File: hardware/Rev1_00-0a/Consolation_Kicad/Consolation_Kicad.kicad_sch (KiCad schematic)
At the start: 35 parts, among them Q14 SSM3K56FS,LF

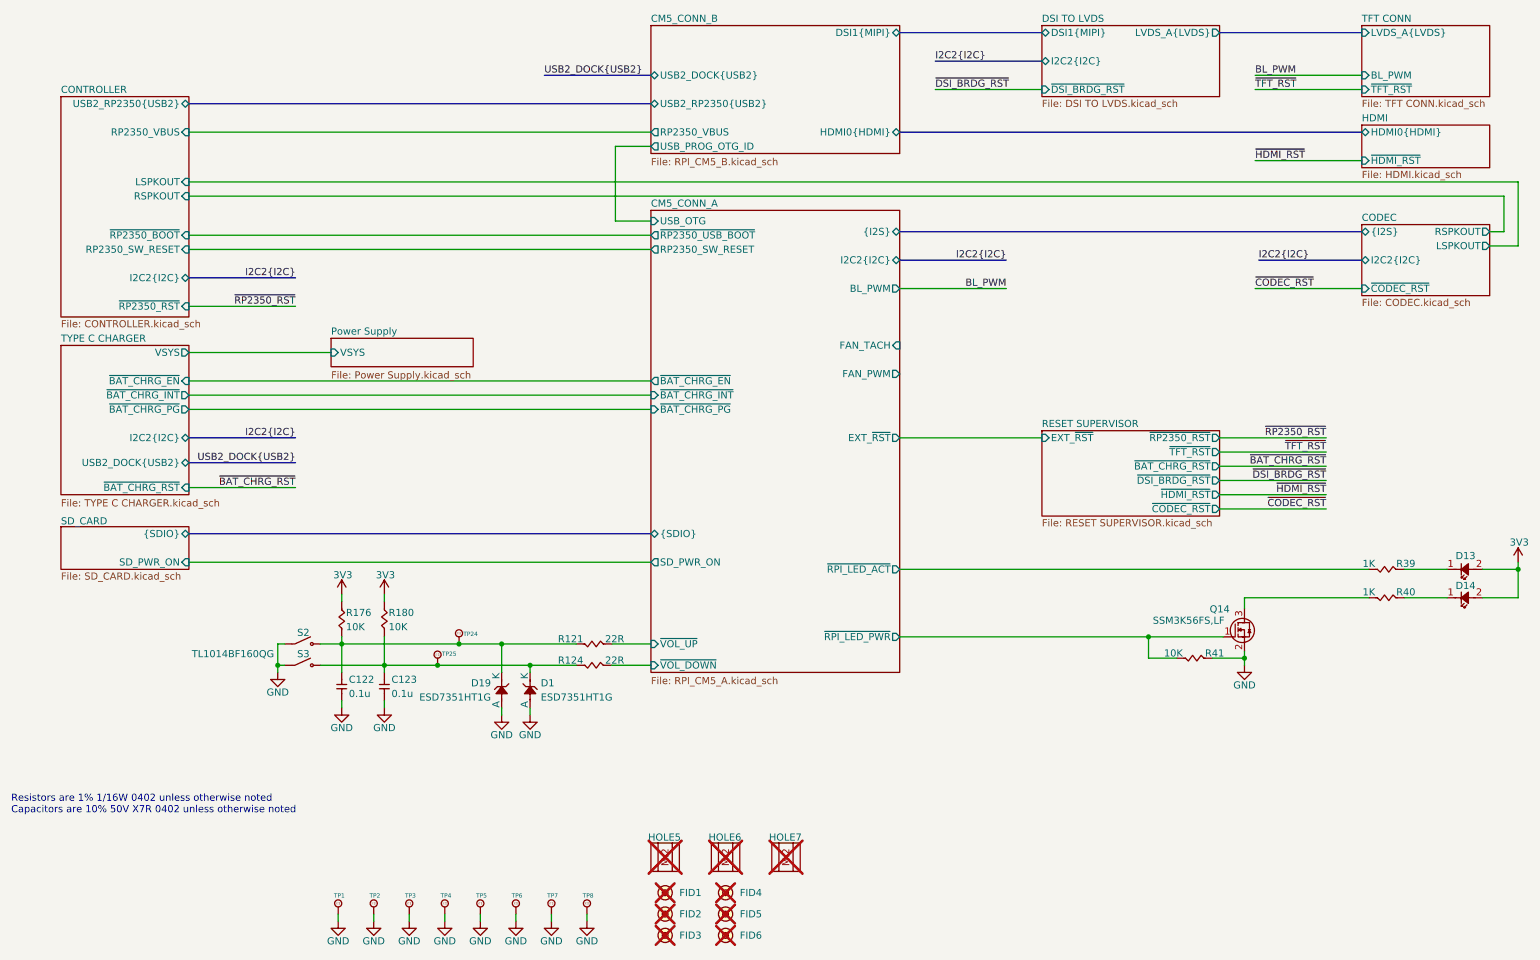
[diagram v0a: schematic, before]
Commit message: Preliminary routing (DiffPairs, Power planes) in progress Slight changes to schematics to accommodate routing
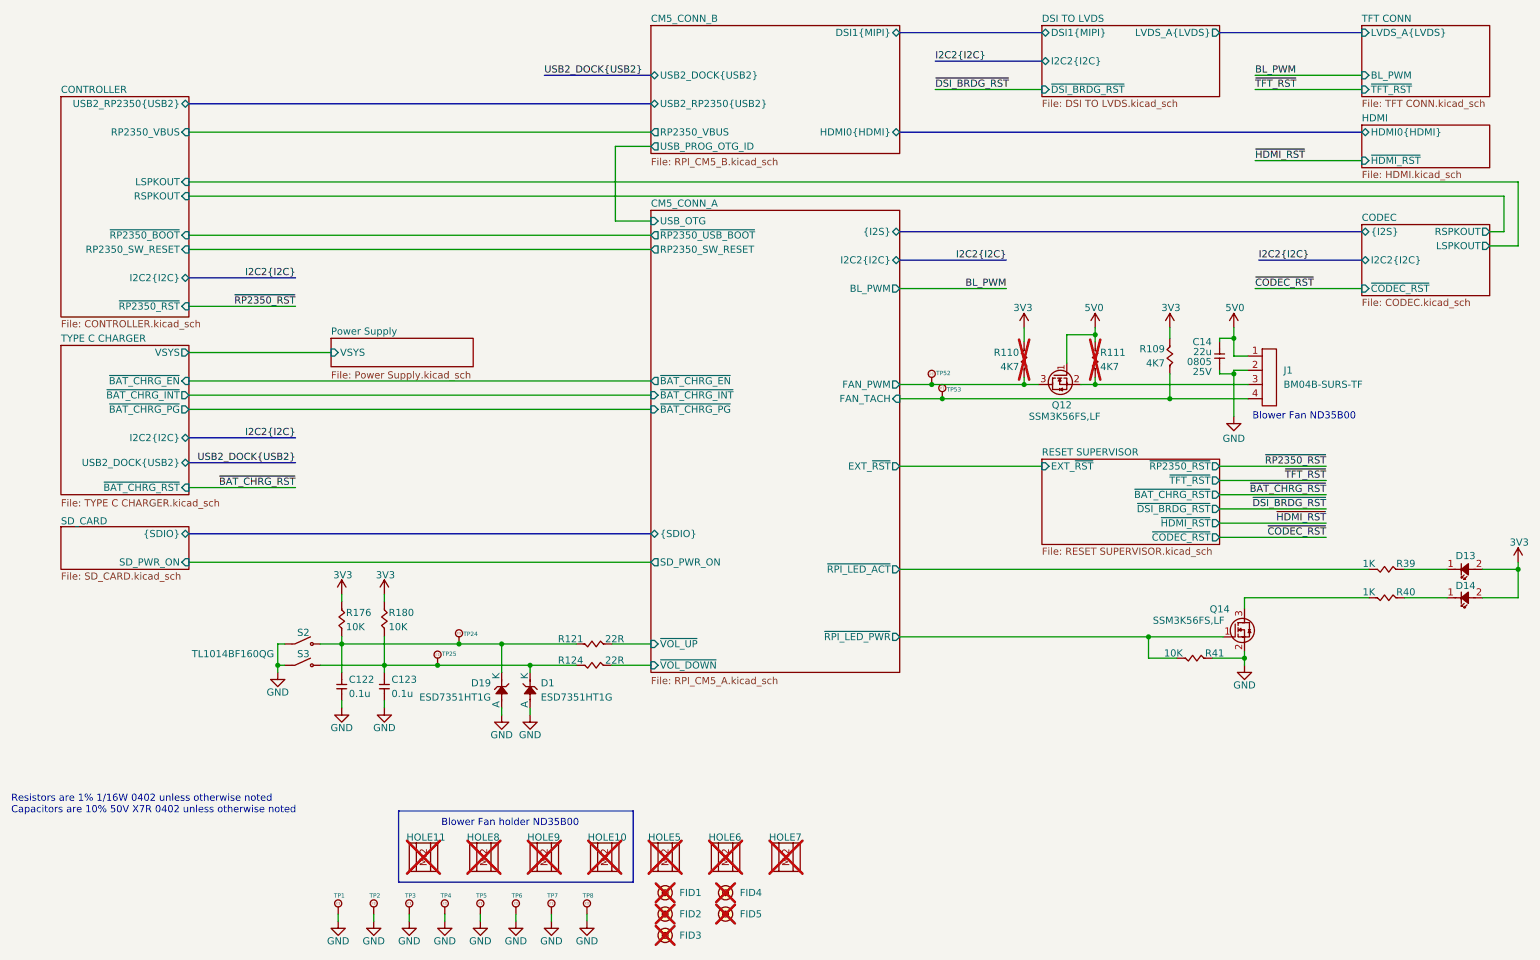
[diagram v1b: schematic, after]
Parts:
- removed FID6: (no value), footprint:FIDUCIAL, symbol KiCad_Lib_Symbols:FIDUCIAL
- added C14: 22u, footprint:CAP_NONPOL_0805, symbol KicadCompDb:Capacitors/CAP_CER_SMT_00011
- added HOLE10, HOLE11, HOLE8, HOLE9: (no value), footprint:NPTH_M2, symbol KiCad_Lib_Symbols:NPTH_M2
- added J1: BM04B-SURS-TF, footprint:BM04B-SURS-TF, symbol KicadCompDb:Connector/CONN_00032
- added Q12: SSM3K56FS,LF, footprint:SC-75, symbol KicadCompDb:Mosfet/MOSFET_00002
- added R109, R110, R111: 4K7, footprint:RES_0402, symbol KicadCompDb:Resistors/RES_SMT_00010
- added TP52, TP53: 75 mils, footprint:SMT_TP_75_MILS, symbol KicadCompDb:Test Point/TP_00004
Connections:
- net 3V3: now also R109.2, R110.2
- net CM5_CONN_A/FAN_PWM: now also Q12.3 (D), R110.1, TP52.1
- net CM5_CONN_A/FAN_TACH: now also J1.4, R109.1, TP53.1
- net GND: now also C14.1, J1.2
- new net: J1.3, Q12.2 (S), R111.1
- new net 5V0: C14.2, J1.1, Q12.1 (G), R111.2
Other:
- note added: "Blower Fan ND35B00"
- note added: "Blower Fan holder ND35B00"

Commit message: Preliminary routing
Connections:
- net 3V3: now also Q12.1 (G)
- net 5V0: no longer Q12.1 (G)
- net CM5_CONN_A/FAN_PWM: now also Q12.2 (S); no longer Q12.3 (D)
- net CM5_CONN_A/~{VOL_DOWN}: now also TP25.1
- net CM5_CONN_A/~{VOL_UP}: now also TP24.1
- net at C122.2, D19.1 (K), R121.2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: no longer TP24.1
- net at C123.2, D1.1 (K), R124.2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: no longer TP25.1
- net at J1.3, R111.1: now also Q12.3 (D); no longer Q12.2 (S)
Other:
- moved on the sheet: Q12, R121, R124

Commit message: Routing Adjust PinMux to ease routing
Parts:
- removed HOLE8: (no value), footprint:NPTH_M2, symbol KiCad_Lib_Symbols:NPTH_M2
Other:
- moved on the sheet: HOLE11
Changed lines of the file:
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@@
 	(title_block
 		(title "Consolation [Console Emulation]")
-		(date "2026-10-12")
+		(date "2026-10-25")
 		(rev "1.00-0A")
 		(comment 1 "Jean-Francois Bilodeau")
@@
 	)
 	(rectangle
-		(start 81.915 172.085)
+		(start 88.9 172.085)
 		(end 123.825 184.785)
 		(stroke
@@
 	(text "Blower Fan holder ND35B00"
 		(exclude_from_sim no)
-		(at 101.854 174.244 0)
+		(at 106.68 174.244 0)
 		(effects
 			(font
@@
 	)
 	(symbol
-		(lib_id "KiCad_Lib_Symbols:NPTH_M2")
-		(at 94.615 177.8 0)
-		(unit 1)
-		(body_style 1)
-		(exclude_from_sim no)
-		(in_bom no)
-		(on_board yes)
-		(in_pos_files yes)
-		(dnp yes)
-		(property "Reference" "HOLE8"
-			(at 94.107 176.784 0)
-			(show_name no)
-			(do_not_autoplace no)
-			(effects
-				(font
-					(size 1.27 1.27)
-				)
-				(justify left)
-			)
-		)
-		(property "Value" ""
-			(at 94.615 177.8 0)
-			(show_name no)
-			(do_not_autoplace no)
-			(effects
-				(font
-					(size 1.27 1.27)
-				)
-			)
-		)
-		(property "Footprint" "footprint:NPTH_M2"
-			(at 98.425 183.896 0)
-			(hide yes)
-			(show_name no)
-			(do_not_autoplace no)
-			(effects
-				(font
-					(size 1.27 1.27)
-				)
-			)
-		)
-		(property "Datasheet" ""
-			(at 94.615 177.8 0)
-			(hide yes)
-			(show_name no)
-			(do_not_autoplace no)
-			(effects
-				(font
-					(size 1.27 1.27)
-				)
-			)
-		)
-		(property "Description" ""
-			(at 94.615 177.8 0)
-			(hide yes)
-			(show_name no)
-			(do_not_autoplace no)
-			(effects
-				(font
-					(size 1.27 1.27)
-				)
-			)
-		)
-		(instances
-			(project "Consolation_Kicad"
-				(path "/b18b5a64-cfe0-4447-acaf-556f3c6e6513"
-					(reference "HOLE8")
-					(unit 1)
-				)
-			)
-		)
-	)
-	(symbol
 		(lib_id "KiCad_Pwr_Symbols:+3V3")
 		(at 206.375 85.725 0)
@@
 	(symbol
 		(lib_id "KiCad_Lib_Symbols:NPTH_M2")
-		(at 83.82 177.8 0)
+		(at 92.71 177.8 0)
 		(unit 1)
 		(body_style 1)
@@
 		(dnp yes)
 		(property "Reference" "HOLE11"
-			(at 83.312 176.784 0)
+			(at 92.202 176.784 0)
 			(show_name no)
 			(do_not_autoplace no)
@@
 		)
 		(property "Value" ""
-			(at 83.82 177.8 0)
+			(at 92.71 177.8 0)
 			(show_name no)
 			(do_not_autoplace no)
@@
 		)
 		(property "Footprint" "footprint:NPTH_M2"
-			(at 87.63 183.896 0)
+			(at 96.52 183.896 0)
 			(hide yes)
 			(show_name no)
@@
 		)
 		(property "Datasheet" ""
-			(at 83.82 177.8 0)
+			(at 92.71 177.8 0)
 			(hide yes)
 			(show_name no)
@@
 		)
 		(property "Description" ""
-			(at 83.82 177.8 0)
+			(at 92.71 177.8 0)
 			(hide yes)
 			(show_name no)

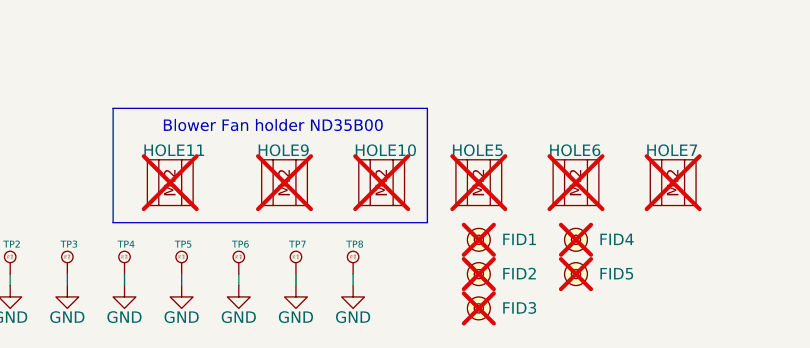
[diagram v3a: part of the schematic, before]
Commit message: Routing + very preliminary design rule check done
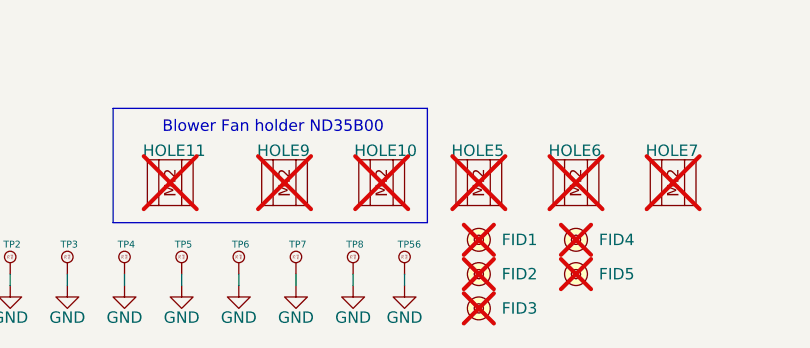
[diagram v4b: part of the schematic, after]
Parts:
- added TP56: 75 mils, footprint:SMT_TP_75_MILS, symbol KicadCompDb:Test Point/TP_00004
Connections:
- net GND: now also TP56.1

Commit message: Add teardrops, clean ERC and DRC check. Review design rules Update fill zones Add stitching vias
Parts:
- FID1, FID2, FID3, FID4, FID5: Component Class (none) -> FIDUCIALS
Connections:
- net at FID1.1: now also FID3.1
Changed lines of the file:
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@@
 	(title_block
 		(title "Consolation [Console Emulation]")
-		(date "2026-10-26")
+		(date "2026-10-27")
 		(rev "1.00-0A")
 		(comment 1 "Jean-Francois Bilodeau")
@@
 		(comment 6 "Jean-Francois Bilodeau")
 		(comment 7 "Not applicable")
-		(comment 8 "In Design")
+		(comment 8 "In DFM Review")
 		(comment 9 "Consolation_1.00-0A_BOM")
 	)
@@
 			)
 		)
-		(property "Component Class" ""
+		(property "Component Class" "FIDUCIALS"
 			(at 129.54 186.69 0)
 			(hide yes)
@@
 			)
 		)
-		(property "Component Class" ""
+		(property "Component Class" "FIDUCIALS"
 			(at 129.54 190.5 0)
 			(hide yes)
@@
 			)
 		)
-		(property "Component Class" ""
+		(property "Component Class" "FIDUCIALS"
 			(at 140.335 190.5 0)
 			(hide yes)
@@
 		(lib_id "KiCad_Lib_Symbols:FIDUCIAL")
 		(at 129.54 194.31 0)
+		(mirror x)
 		(unit 1)
 		(body_style 1)
@@
 		(fields_autoplaced yes)
 		(property "Reference" "FID3"
-			(at 132.08 194.3099 0)
+			(at 132.08 194.3101 0)
 			(show_name no)
 			(do_not_autoplace no)
@@
 			)
 		)
-		(property "Component Class" ""
+		(property "Component Class" "FIDUCIALS"
 			(at 129.54 194.31 0)
 			(hide yes)
@@
 			)
 		)
-		(property "Component Class" ""
+		(property "Component Class" "FIDUCIALS"
 			(at 140.335 186.69 0)
 			(hide yes)

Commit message: Add preliminary manufacturing files for Consolation Review pinout & design notes
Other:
- note added: "Compatible only with CM5"
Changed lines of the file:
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@@
 	(title_block
 		(title "Consolation [Console Emulation]")
-		(date "2026-10-27")
+		(date "2026-10-31")
 		(rev "1.00-0A")
 		(comment 1 "Jean-Francois Bilodeau")
@@
 		)
 	)
+	(text "Compatible only with CM5"
+		(exclude_from_sim no)
+		(at 148.336 152.146 0)
+		(effects
+			(font
+				(size 1.27 1.27)
+				(color 255 153 0 1)
+			)
+		)
+	)

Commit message: Work on DFM, Pick N Place file accuracy, BOM accuracy Generating output files regularly through incremental updates
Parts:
- TP1, TP2, TP24, TP25, TP3, TP4, TP5, TP52, TP53, TP56, TP6, TP7, TP8: now left out of the parts list
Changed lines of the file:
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@@
 		(body_style 1)
 		(exclude_from_sim no)
-		(in_bom yes)
+		(in_bom no)
 		(on_board yes)
-		(in_pos_files yes)
+		(in_pos_files no)
 		(dnp no)
 		(property "Reference" "TP25"
@@
 		(body_style 1)
 		(exclude_from_sim no)
-		(in_bom yes)
+		(in_bom no)
 		(on_board yes)
-		(in_pos_files yes)
+		(in_pos_files no)
 		(dnp no)
 		(property "Reference" "TP7"
@@
 		(body_style 1)
 		(exclude_from_sim no)
-		(in_bom yes)
+		(in_bom no)
 		(on_board yes)
-		(in_pos_files yes)
+		(in_pos_files no)
 		(dnp no)
 		(property "Reference" "TP4"
@@
 		(in_bom no)
 		(on_board yes)
-		(in_pos_files yes)
+		(in_pos_files no)
 		(dnp yes)
 		(property "Reference" "HOLE5"
@@
 		(in_bom no)
 		(on_board yes)
-		(in_pos_files yes)
+		(in_pos_files no)
 		(dnp yes)
 		(fields_autoplaced yes)
@@
 		(body_style 1)
 		(exclude_from_sim no)
-		(in_bom yes)
+		(in_bom no)
 		(on_board yes)
-		(in_pos_files yes)
+		(in_pos_files no)
 		(dnp no)
 		(property "Reference" "TP3"
@@
 		(in_bom no)
 		(on_board yes)
-		(in_pos_files yes)
+		(in_pos_files no)
 		(dnp yes)
 		(property "Reference" "HOLE6"
@@
 		(body_style 1)
 		(exclude_from_sim no)
-		(in_bom yes)
+		(in_bom no)
 		(on_board yes)
-		(in_pos_files yes)
+		(in_pos_files no)
 		(dnp no)
 		(property "Reference" "TP52"
@@
 		(in_bom no)
 		(on_board yes)
-		(in_pos_files yes)
+		(in_pos_files no)
 		(dnp yes)
 		(fields_autoplaced yes)
@@
 		(body_style 1)
 		(exclude_from_sim no)
-		(in_bom yes)
+		(in_bom no)
 		(on_board yes)
-		(in_pos_files yes)
+		(in_pos_files no)
 		(dnp no)
 		(property "Reference" "TP56"
@@
 		(in_bom no)
 		(on_board yes)
-		(in_pos_files yes)
+		(in_pos_files no)
 		(dnp yes)
 		(fields_autoplaced yes)
@@
 		(in_bom no)
 		(on_board yes)
-		(in_pos_files yes)
+		(in_pos_files no)
 		(dnp yes)
 		(property "Reference" "HOLE7"
@@
 		(body_style 1)
 		(exclude_from_sim no)
-		(in_bom yes)
+		(in_bom no)
 		(on_board yes)
-		(in_pos_files yes)
+		(in_pos_files no)
 		(dnp no)
 		(property "Reference" "TP1"
@@
 		(in_bom no)
 		(on_board yes)
-		(in_pos_files yes)
+		(in_pos_files no)
 		(dnp yes)
 		(property "Reference" "HOLE9"
@@
 		(body_style 1)
 		(exclude_from_sim no)
-		(in_bom yes)
+		(in_bom no)
 		(on_board yes)
-		(in_pos_files yes)
+		(in_pos_files no)
 		(dnp no)
 		(property "Reference" "TP6"
@@
 		(body_style 1)
 		(exclude_from_sim no)
-		(in_bom yes)
+		(in_bom no)
 		(on_board yes)
-		(in_pos_files yes)
+		(in_pos_files no)
 		(dnp no)
 		(property "Reference" "TP24"
@@
 		(body_style 1)
 		(exclude_from_sim no)
-		(in_bom yes)
+		(in_bom no)
 		(on_board yes)
-		(in_pos_files yes)
+		(in_pos_files no)
 		(dnp no)
 		(property "Reference" "TP5"
@@
 		(in_bom no)
 		(on_board yes)
-		(in_pos_files yes)
+		(in_pos_files no)
 		(dnp yes)
 		(property "Reference" "HOLE10"
@@
 		(in_bom no)
 		(on_board yes)
-		(in_pos_files yes)
+		(in_pos_files no)
 		(dnp yes)
 		(fields_autoplaced yes)
@@
 		(body_style 1)
 		(exclude_from_sim no)
-		(in_bom yes)
+		(in_bom no)
 		(on_board yes)
-		(in_pos_files yes)
+		(in_pos_files no)
 		(dnp no)
 		(property "Reference" "TP53"
@@
 		(body_style 1)
 		(exclude_from_sim no)
-		(in_bom yes)
+		(in_bom no)
 		(on_board yes)
-		(in_pos_files yes)
+		(in_pos_files no)
 		(dnp no)
 		(property "Reference" "TP8"
@@
 		(body_style 1)
 		(exclude_from_sim no)
-		(in_bom yes)
+		(in_bom no)
 		(on_board yes)
-		(in_pos_files yes)
+		(in_pos_files no)
 		(dnp no)
 		(property "Reference" "TP2"
@@
 		(in_bom no)
 		(on_board yes)
-		(in_pos_files yes)
+		(in_pos_files no)
 		(dnp yes)
 		(property "Reference" "HOLE11"
@@
 		(in_bom no)
 		(on_board yes)
-		(in_pos_files yes)
+		(in_pos_files no)
 		(dnp yes)
 		(fields_autoplaced yes)
